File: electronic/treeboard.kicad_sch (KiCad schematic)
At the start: 101 parts, among them J12 Conn_02x10_Counter_Clockwise, J2 Conn_01x06_MountingPin, J3 Conn_01x06_MountingPin, J4 USB_C_Receptacle_USB2.0, J5 Conn_01x06_Socket, J6 Conn_01x06_Socket, J7 Conn_01x06_Socket, J8 Conn_02x10_Counter_Clockwise, J9 Conn_02x05_Odd_Even, SW1 SW_Push_45deg, SW10 SW_Push_45deg, SW11 SW_Push_45deg, SW12 SW_Push_45deg, SW13 SW_Push_45deg, SW14 SW_Push_45deg, SW15 SW_Push_45deg, SW16 SW_Push_45deg, SW17 SW_Push_45deg, SW18 SW_Push_45deg, SW19 SW_Push_45deg, SW2 SW_Push_45deg, SW20 RotaryEncoder, SW3 SW_Push_45deg, SW4 SW_Push_45deg, SW5 SW_Push_45deg, SW6 SW_Push_45deg, SW7 SW_Push_45deg, SW8 SW_Push_45deg, SW9 SW_Push_45deg, U1 TXB0104RUT, U6 BMD-340-A-R, U7 TXB0104RUT, Y2 32.064kHz

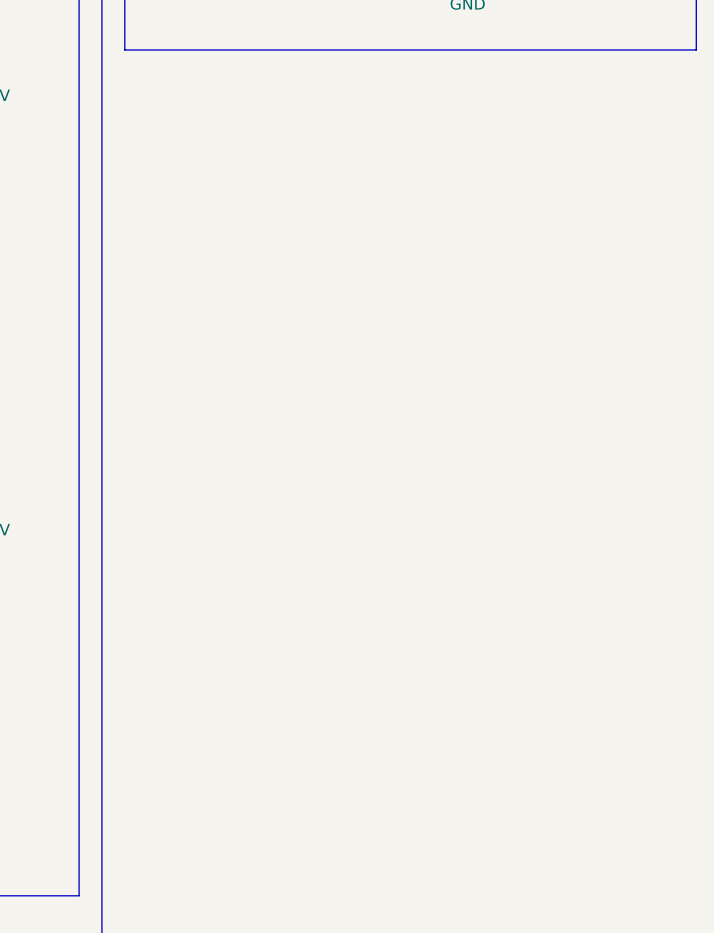
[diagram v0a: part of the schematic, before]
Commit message: backup before switch
switching to nrf52840 feather
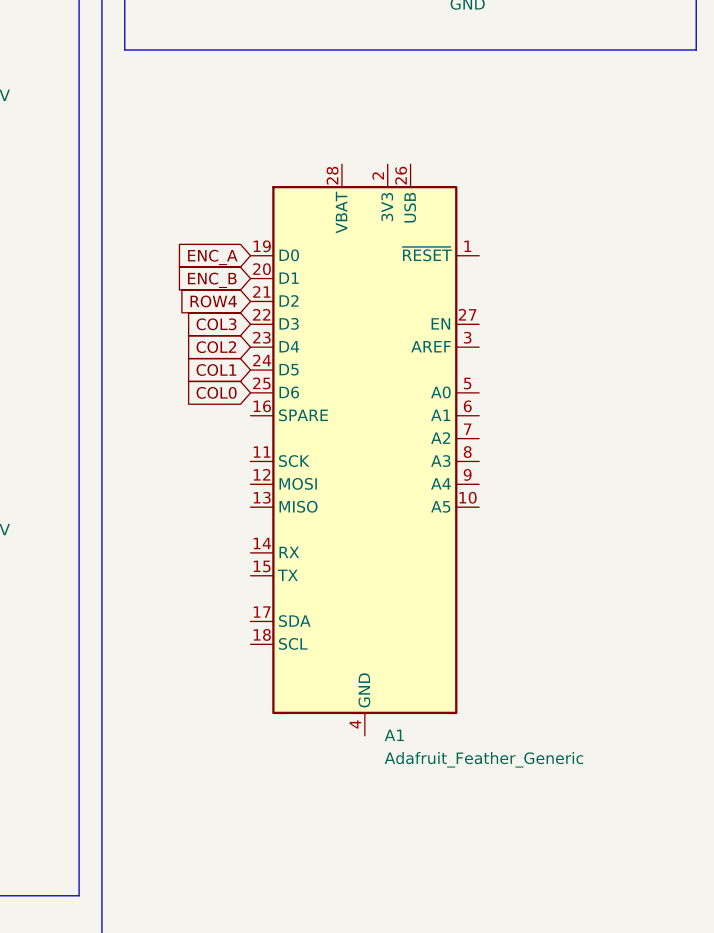
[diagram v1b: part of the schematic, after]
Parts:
- added A1: Adafruit_Feather_Generic, Module:Adafruit_Feather, symbol MCU_Module:Adafruit_Feather_Generic
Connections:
- net COL0: now also A1.25 (D6)
- net COL1: now also A1.24 (D5)
- net COL2: now also A1.23 (D4)
- net COL3: now also A1.22 (D3)
- net ENC_A: now also A1.19 (D0)
- net ENC_B: now also A1.20 (D1)
- net ROW4: now also A1.21 (D2)
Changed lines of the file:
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@@
     (effects (font (size 1.27 1.27)) (justify left bottom))
   )
+  (global_label "COL0" (shape input) (at 307.34 142.24 180) (fields_autoplaced)
+    (effects (font (size 1.27 1.27)) (justify right))
+    (property "Intersheetrefs" "${INTERSHEET_REFS}" (at 299.5167 142.24 0)
+      (effects (font (size 1.27 1.27)) (justify right) hide)
+    )
+  )
   (global_label "SWCLK" (shape input) (at 209.55 120.65 0) (fields_autoplaced)
     (effects (font (size 1.27 1.27)) (justify left))
@@
     )
   )
+  (global_label "COL1" (shape input) (at 307.34 139.7 180) (fields_autoplaced)
+    (effects (font (size 1.27 1.27)) (justify right))
+    (property "Intersheetrefs" "${INTERSHEET_REFS}" (at 299.5167 139.7 0)
+      (effects (font (size 1.27 1.27)) (justify right) hide)
+    )
+  )
   (global_label "P0_1" (shape input) (at 209.55 138.43 0) (fields_autoplaced)
     (effects (font (size 1.27 1.27)) (justify left))
@@
     )
   )
+  (global_label "COL3" (shape input) (at 307.34 134.62 180) (fields_autoplaced)
+    (effects (font (size 1.27 1.27)) (justify right))
+    (property "Intersheetrefs" "${INTERSHEET_REFS}" (at 299.5167 134.62 0)
+      (effects (font (size 1.27 1.27)) (justify right) hide)
+    )
+  )
+  (global_label "ROW4" (shape input) (at 307.34 132.08 180) (fields_autoplaced)
+    (effects (font (size 1.27 1.27)) (justify right))
+    (property "Intersheetrefs" "${INTERSHEET_REFS}" (at 299.0934 132.08 0)
+      (effects (font (size 1.27 1.27)) (justify right) hide)
+    )
+  )
   (global_label "RGB_CTRL" (shape input) (at 59.69 218.44 180) (fields_autoplaced)
     (effects (font (size 1.27 1.27)) (justify right))
@@
     )
   )
+  (global_label "ENC_A" (shape input) (at 307.34 127 180) (fields_autoplaced)
+    (effects (font (size 1.27 1.27)) (justify right))
+    (property "Intersheetrefs" "${INTERSHEET_REFS}" (at 298.5491 127 0)
+      (effects (font (size 1.27 1.27)) (justify right) hide)
+    )
+  )
   (global_label "ENC_A" (shape input) (at 96.52 113.03 0) (fields_autoplaced)
     (effects (font (size 1.27 1.27)) (justify left))
@@
     )
   )
+  (global_label "ENC_B" (shape input) (at 307.34 129.54 180) (fields_autoplaced)
+    (effects (font (size 1.27 1.27)) (justify right))
+    (property "Intersheetrefs" "${INTERSHEET_REFS}" (at 298.3677 129.54 0)
+      (effects (font (size 1.27 1.27)) (justify right) hide)
+    )
+  )
   (global_label "ROW2" (shape input) (at 72.39 215.9 0) (fields_autoplaced)
     (effects (font (size 1.27 1.27)) (justify left))
@@
     (effects (font (size 1.27 1.27)) (justify right))
     (property "Intersheetrefs" "${INTERSHEET_REFS}" (at 232.3882 172.72 0)
+      (effects (font (size 1.27 1.27)) (justify right) hide)
+    )
+  )
+  (global_label "COL2" (shape input) (at 307.34 137.16 180) (fields_autoplaced)
+    (effects (font (size 1.27 1.27)) (justify right))
+    (property "Intersheetrefs" "${INTERSHEET_REFS}" (at 299.5167 137.16 0)
       (effects (font (size 1.27 1.27)) (justify right) hide)
     )
@@
         )
       )
+    )
+  )
+  (symbol (lib_id "MCU_Module:Adafruit_Feather_Generic") (at 320.04 147.32 0) (unit 1)
+    (in_bom yes) (on_board yes) (dnp no) (fields_autoplaced)
+    (property "Reference" "A1" (at 322.2341 180.34 0)
+      (effects (font (size 1.27 1.27)) (justify left))
+    )
+    (property "Value" "Adafruit_Feather_Generic" (at 322.2341 182.88 0)
+      (effects (font (size 1.27 1.27)) (justify left))
+    )
+    (property "Footprint" "Module:Adafruit_Feather" (at 322.58 181.61 0)
+      (effects (font (size 1.27 1.27)) (justify left) hide)
+    )
+    (property "Datasheet" "https://cdn-learn.adafruit.com/downloads/pdf/adafruit-feather.pdf" (at 320.04 167.64 0)
+      (effects (font (size 1.27 1.27)) hide)
+    )
+    (pin "17")
+    (pin "26")
+    (pin "24")
+    (pin "28")
+    (pin "23")
+    (pin "19")
+    (pin "10")
+    (pin "22")
+    (pin "18")
+    (pin "20")
+    (pin "13")
+    (pin "8")
+    (pin "1")
+    (pin "2")
+    (pin "25")
+    (pin "3")
+    (pin "4")
+    (pin "15")
+    (pin "14")
+    (pin "21")
+    (pin "6")
+    (pin "12")
+    (pin "7")
+    (pin "9")
+    (pin "16")
+    (pin "11")
+    (pin "27")
+    (pin "5")
+    (instances
+      (project "treeboard"
+        (path "/1f257e0a-26b9-4058-b875-d54df1a4562a"
+          (reference "A1") (unit 1)
+        )
+      )
